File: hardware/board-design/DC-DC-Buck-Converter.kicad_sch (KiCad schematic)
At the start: 0 parts

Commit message: hw(schematic): complete Buck Converter schematic design
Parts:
- added C1, C3: 10uF, symbol Device:C
- added C2: 1OuF, symbol Device:C
- added C_BOOTSTRAP_1: 0.1µF, symbol Device:C
- added L1: 10uH, symbol Device:L
- added Q_HIGH_1, Q_LOW_1: Q_NMOS, symbol Device:Q_NMOS
- added R_GATE_1, R_GATE_2: 10, symbol Device:R
- added R_GATE_3, R_GATE_4: 100k, symbol Device:R
- added R_LOAD_1, R_LOAD_2: 1K, symbol Device:R
- added U1: Half-Bridge Gate Driver, Custom-lib:SON8 (DRM) (4 mm × 4 mm), symbol Driver_FET:Custom-GateDRVR
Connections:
- new net: C3.1, U1.1 (VDD)
- new net: C_BOOTSTRAP_1.1, U1.2 (HB)
- new net: R_GATE_1.1, U1.3 (HO)
- new net: C_BOOTSTRAP_1.2, L1.1, Q_HIGH_1.S, Q_LOW_1.D, R_GATE_3.2, U1.4 (HS)
- new net: R_GATE_2.1, U1.8 (LO)
- new net: C2.1, L1.2, R_LOAD_2.2
- new net: Q_LOW_1.G, R_GATE_2.2, R_GATE_4.1
- new net: Q_HIGH_1.G, R_GATE_1.2, R_GATE_3.1
- new net GND: C1.2, C2.2, C3.2, Q_LOW_1.S, R_GATE_4.2, R_LOAD_1.1, U1.7 (VSS), U1.9 (EP)
- new net V_INPUT: C1.1, Q_HIGH_1.D
- new net V_OUT: R_LOAD_1.2, R_LOAD_2.1
- no-connect marks 0 -> 2

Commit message: hw(schematic): update schematic and finally complate ()
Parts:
- added C4, C5, C6: 0.1uF, symbol Device:C
- R_LOAD_1: value 1K -> 47k
- R_LOAD_2: value 1K -> 10k
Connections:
- net GND: now also R_LOAD_2.1, C4.2, C6.2; no longer R_LOAD_1.1
- net V_INPUT: now also C4.1
- net V_OUT: now also C2.1, L1.2, C6.1; no longer R_LOAD_2.1
- net VDD: now reaches C3.1, U1.1 (VDD)
- net VDD: now also C5.1
- new net mcu_input: R_LOAD_1.1, R_LOAD_2.2
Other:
- moved on the sheet: R_LOAD_1

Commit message: feat(footprint): add footprints for Capacitors and MOSFETs
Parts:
- C1, C2, C3: footprint (none) -> Capacitor_Tantalum_SMD:CP_EIA-7343-30_AVX-N_HandSolder
- C4, C5, C6, C_BOOTSTRAP_1: footprint (none) -> Capacitor_SMD:C_0402_1005Metric_Pad0.74x0.62mm_HandSolder
- Q_HIGH_1, Q_LOW_1: footprint (none) -> Package_SON:VSONP-8-1EP_5x6_P1.27mm
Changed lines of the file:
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@@
 			)
 		)
-		(property "Footprint" ""
+		(property "Footprint" "Capacitor_Tantalum_SMD:CP_EIA-7343-30_AVX-N_HandSolder"
 			(at 143.2052 91.44 0)
 			(hide yes)
@@
 			)
 		)
-		(property "Footprint" ""
+		(property "Footprint" "Capacitor_Tantalum_SMD:CP_EIA-7343-30_AVX-N_HandSolder"
 			(at 102.5652 110.49 0)
 			(hide yes)
@@
 			)
 		)
-		(property "Footprint" ""
+		(property "Footprint" "Package_SON:VSONP-8-1EP_5x6_P1.27mm"
 			(at 132.08 92.71 0)
 			(hide yes)
@@
 			)
 		)
-		(property "Footprint" ""
+		(property "Footprint" "Capacitor_Tantalum_SMD:CP_EIA-7343-30_AVX-N_HandSolder"
 			(at 117.8052 91.44 0)
 			(hide yes)
@@
 			)
 		)
-		(property "Footprint" ""
+		(property "Footprint" "Capacitor_SMD:C_0402_1005Metric_Pad0.74x0.62mm_HandSolder"
 			(at 149.5552 91.44 0)
 			(hide yes)
@@
 			)
 		)
-		(property "Footprint" ""
+		(property "Footprint" "Capacitor_SMD:C_0402_1005Metric_Pad0.74x0.62mm_HandSolder"
 			(at 93.6752 110.49 0)
 			(hide yes)
@@
 			)
 		)
-		(property "Footprint" ""
+		(property "Footprint" "Capacitor_SMD:C_0402_1005Metric_Pad0.74x0.62mm_HandSolder"
 			(at 111.4552 91.44 0)
 			(hide yes)
@@
 			)
 		)
-		(property "Footprint" ""
+		(property "Footprint" "Package_SON:VSONP-8-1EP_5x6_P1.27mm"
 			(at 119.38 81.28 0)
 			(hide yes)
@@
 			)
 		)
-		(property "Footprint" ""
+		(property "Footprint" "Capacitor_SMD:C_0402_1005Metric_Pad0.74x0.62mm_HandSolder"
 			(at 118.11 94.2848 0)
 			(hide yes)

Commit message: feat(BOM): add part number and manufacturer name for capacitors and mosfets
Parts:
- C1, C2, C3: Manufacturer (none) -> Vishay; PART NUMBER (none) -> TR3D106K050C0550
- C4, C5, C6, C_BOOTSTRAP_1: Manufacturer (none) -> Vishay; PART NUMBER (none) -> VJ0402Y104KXACW1BC
- Q_HIGH_1, Q_LOW_1: Manufacturer (none) -> Texas Insturements; PART NUMBER (none) -> CSD19532Q5B
- U1: Manufacturer (none) -> Texas Insturements; PART NUMBER (none) -> UCC27284

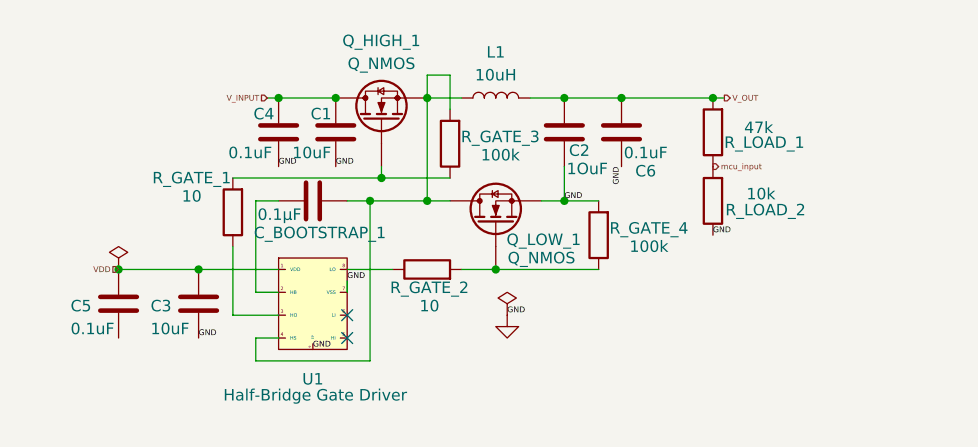
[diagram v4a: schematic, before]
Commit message: add new values and information to fields and
Updated and rearranged the schema.
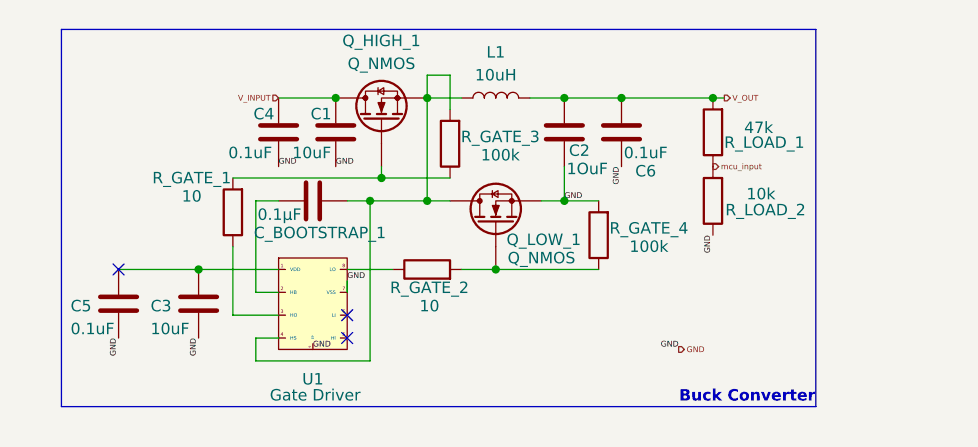
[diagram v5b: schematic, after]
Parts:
- C1, C2, C3: footprint Capacitor_Tantalum_SMD:CP_EIA-7343-30_AVX-N_HandSolder -> Custom-lib:CAPC6153X390N; Manufacturer Vishay -> Murata; PART NUMBER TR3D106K050C0550 -> KRM55QR72A106KH01L
- C4, C5, C6, C_BOOTSTRAP_1: footprint Capacitor_SMD:C_0402_1005Metric_Pad0.74x0.62mm_HandSolder -> Capacitor_SMD:C_0603_1608Metric_Pad1.08x0.95mm_HandSolder; Manufacturer Vishay -> Murata; PART NUMBER VJ0402Y104KXACW1BC -> GRM188R72A104KA35D
- L1: footprint (none) -> Custom-lib:WE-HCI_2212; Manufacturer (none) -> Würth Elektronik; PART NUMBER (none) -> 74435581000
- R_GATE_1, R_GATE_2: footprint (none) -> Resistor_SMD:R_0603_1608Metric_Pad0.98x0.95mm_HandSolder; Manufacturer (none) -> Vishay; PART NUMBER (none) -> CRCW060310R0FKEA
- R_GATE_3, R_GATE_4: footprint (none) -> Resistor_SMD:R_0402_1005Metric_Pad0.72x0.64mm_HandSolder; Manufacturer (none) -> Vishay; PART NUMBER (none) -> CRCW0402100KFKED
- R_LOAD_1: footprint (none) -> Resistor_SMD:R_0603_1608Metric_Pad0.98x0.95mm_HandSolder; Manufacturer (none) -> Vishay; PART NUMBER (none) -> CRCW060347K0FKEA
- R_LOAD_2: footprint (none) -> Resistor_SMD:R_0402_1005Metric_Pad0.72x0.64mm_HandSolder; Manufacturer (none) -> Vishay; PART NUMBER (none) -> CRCW040210K0FKED
- U1: value Half-Bridge Gate Driver -> Gate Driver
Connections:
- net GND: now also C5.2
- net VDD: no longer names the net of C3.1, C5.1, U1.1 (VDD)
- no-connect marks 2 -> 3
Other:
- note added: "Buck Converter"

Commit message: feat(schematic): add a regulator for the gate driver
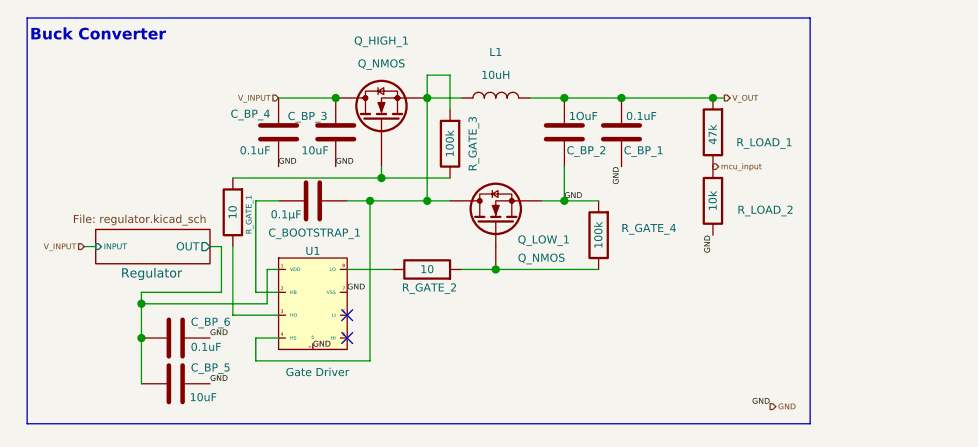
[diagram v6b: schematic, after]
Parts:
- removed C3: 10uF, Custom-lib:CAPC6153X390N, symbol Device:C
- removed C5: 0.1uF, Capacitor_SMD:C_0603_1608Metric_Pad1.08x0.95mm_HandSolder, symbol Device:C
- added C_BP_5: 10uF, Custom-lib:CAPC6153X390N, symbol Device:C
- added C_BP_6: 0.1uF, Capacitor_SMD:C_0603_1608Metric_Pad1.08x0.95mm_HandSolder, symbol Device:C
- renumbered C6 to C_BP_1, C2 to C_BP_2, C1 to C_BP_3, C4 to C_BP_4
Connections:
- net GND: now also C_BP_5.2, C_BP_6.2
- net Regulator/OUT: now reaches U1.1 (VDD)
- net Regulator/OUT: now also C_BP_5.1, C_BP_6.1
- no-connect marks 3 -> 2
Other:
- added sheet Regulator (regulator.kicad_sch)

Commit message: feat(schematic): define footprint and  part number
for regulator circuit
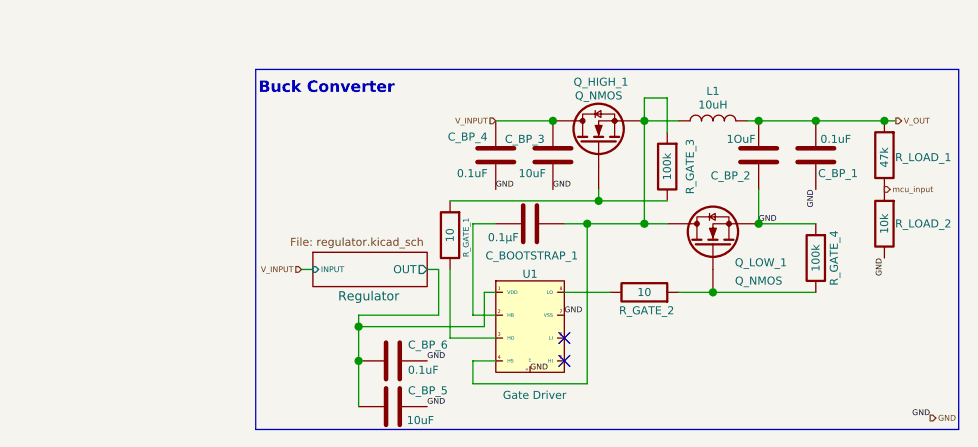
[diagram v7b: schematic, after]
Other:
- moved on the sheet: C_BOOTSTRAP_1, C_BP_1, C_BP_2, C_BP_3, C_BP_4, C_BP_5, C_BP_6, L1, Q_HIGH_1, Q_LOW_1, R_GATE_1, R_GATE_2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

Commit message: feat(schematic): update schematic
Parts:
- added D4: D, symbol Device:D
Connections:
- net Regulator/OUT: now also D4.2 (A)
- net at C_BOOTSTRAP_1.1, U1.2 (HB): now also D4.1 (K)
- net mcu_input renamed mcu_output
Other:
- moved on the sheet: R_GATE_1
